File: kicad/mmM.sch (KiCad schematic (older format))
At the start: 29 parts, among them P1 AREF, P4 ICSP, P5 FTDI, SW1 Reset, SW2 INT0, SW3 INT1, U7 ATMEGA328P-AU-ND, X1 16MHz

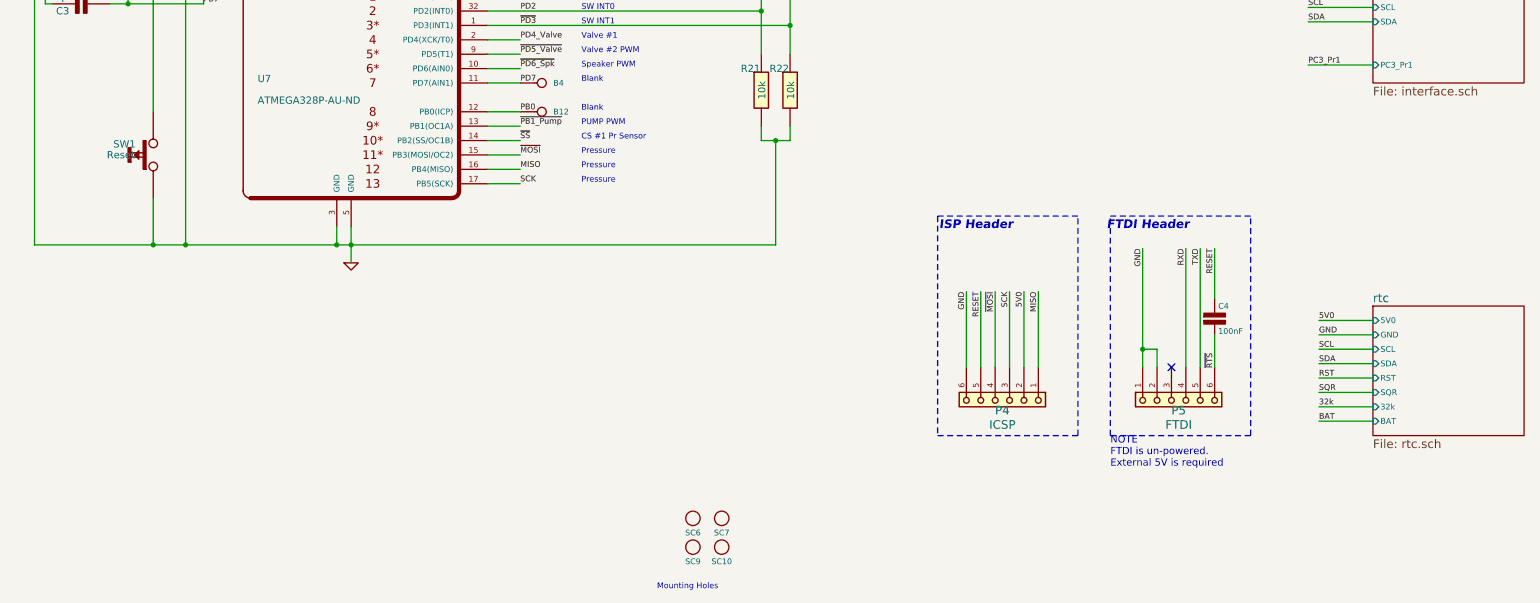
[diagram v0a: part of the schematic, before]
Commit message: added Cap across RST sw. Fresh Gerbers, PDF. Final v1 ready for prototype
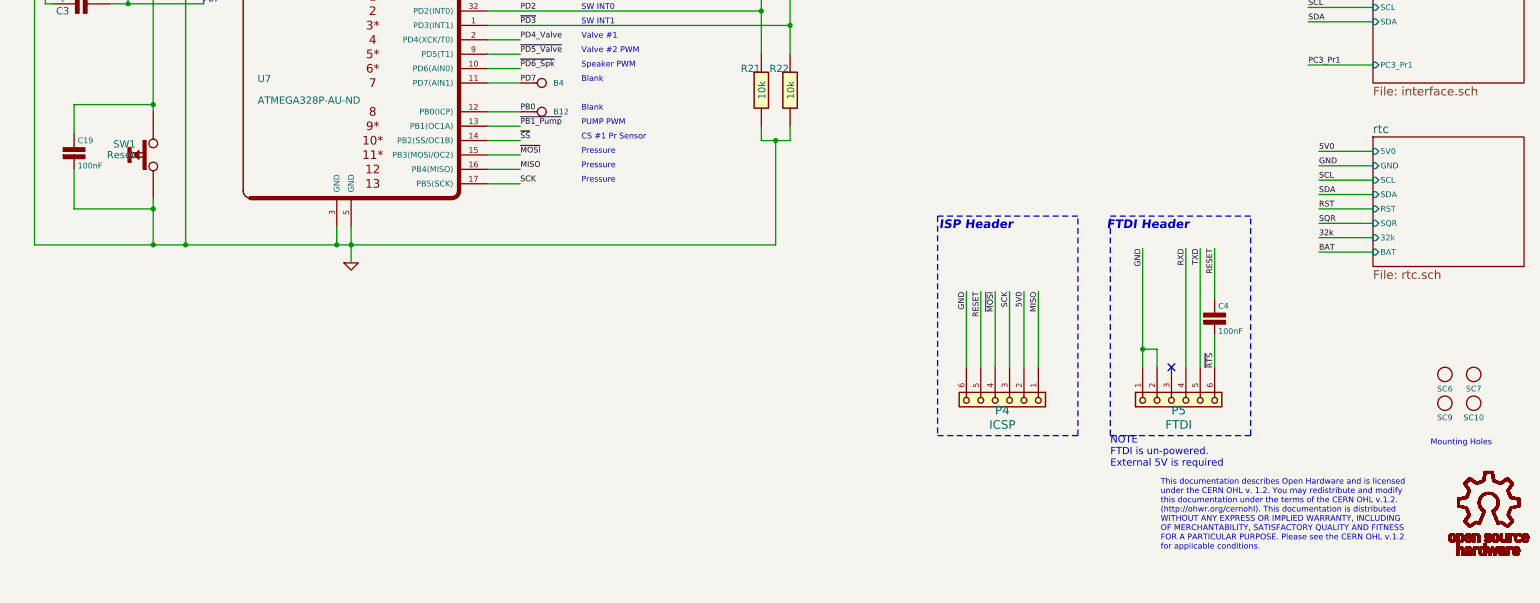
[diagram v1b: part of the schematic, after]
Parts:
- added C19: 100nF, mmM:c_0805, symbol C
- added M1: OSHW-LOGO, OSHW-LOGO, symbol OSHW-LOGO
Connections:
- net GND: now also C19.2
- net RESET: now also C19.1
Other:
- note added: "This documentation describes Open Hardware and is licensed \nunder the CERN OHL v. 1.2. You may redistribute and modify \nthis documentation under the terms of the CERN OHL v.1.2. \n(http://ohwr.org/cernohl). This documentation is distributed\nWITHOUT ANY EXPRESS OR IMPLIED WARRANTY, INCLUDING \nOF MERCHANTABILITY, SATISFACTORY QUALITY AND FITNESS\nFOR A PARTICULAR PURPOSE. Please see the CERN OH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"
- moved on the sheet: SC10, SC6, SC7, SC9
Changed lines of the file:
@@
 encoding utf-8
 Sheet 1 4
-Title "uControl_mini"
-Date "2015 July 09, Thursday"
+Title "mmMercury : Blood Pressure Measurement Platform"
+Date "2015-12-27"
 Rev "1"
 Comp "WyoLum"
@@
 Text Notes 4550 3450 0    40   ~ 0
 SW INT1
-Text Notes 5075 7375 0    40   ~ 0
+Text Notes 10450 6375 0    40   ~ 0
 Mounting Holes
 Text Label 9775 825  0    40   ~ 0
@@
 $EndSheet
 $Sheet
-S 10050 5400 1050 900
+S 10050 4225 1050 900
 U 4E1FEA4E
 F0 "rtc" 60
 F1 "rtc.sch" 60
-F2 "GND" I L 10050 5600 40
-F3 "SDA" I L 10050 5800 40
-F4 "SCL" I L 10050 5700 40
-F5 "5V0" I L 10050 5500 40
-F6 "RST" I L 10050 5900 40
-F7 "32k" I L 10050 6100 40
-F8 "BAT" I L 10050 6200 40
-F9 "SQR" I L 10050 6000 40
+F2 "GND" I L 10050 4425 40
+F3 "SDA" I L 10050 4625 40
+F4 "SCL" I L 10050 4525 40
+F5 "5V0" I L 10050 4325 40
+F6 "RST" I L 10050 4725 40
+F7 "32k" I L 10050 4925 40
+F8 "BAT" I L 10050 5025 40
+F9 "SQR" I L 10050 4825 40
 $EndSheet
 Text Label 1025 2550 0    40   ~ 0
@@
 PB6
 $Comp
-L GND #PWR01
+L GND #PWR3
 U 1 1 4F5AFC62
 P 2950 5100
-F 0 "#PWR01" H 2950 5100 30  0001 C CNN
+F 0 "#PWR3" H 2950 5100 30  0001 C CNN
 F 1 "GND" H 2950 5030 30  0001 C CNN
 F 2 "" H 2950 5100 60  0001 C CNN
@@
 	1    0    0    -1
 $EndComp
-Text Label 9675 6200 0    40   ~ 0
+Text Label 9675 5025 0    40   ~ 0
 BAT
-Text Label 9675 6100 0    40   ~ 0
+Text Label 9675 4925 0    40   ~ 0
 32k
-Text Label 9675 6000 0    40   ~ 0
+Text Label 9675 4825 0    40   ~ 0
 SQR
-Text Label 9675 5900 0    40   ~ 0
+Text Label 9675 4725 0    40   ~ 0
 RST
-Text Label 9675 5600 0    40   ~ 0
+Text Label 9675 4425 0    40   ~ 0
 GND
-Text Label 9675 5800 0    40   ~ 0
+Text Label 9675 4625 0    40   ~ 0
 SDA
-Text Label 9675 5700 0    40   ~ 0
+Text Label 9675 4525 0    40   ~ 0
 SCL
-Text Label 9675 5500 0    40   ~ 0
+Text Label 9675 4325 0    40   ~ 0
 5V0
 Text Label 1575 2250 1    40   ~ 0
@@
 Blank
 $Comp
-L PWR_FLAG #FLG02
+L PWR_FLAG #FLG1
 U 1 1 520CA632
 P 725 2475
-F 0 "#FLG02" H 725 2745 30  0001 C CNN
+F 0 "#FLG1" H 725 2745 30  0001 C CNN
 F 1 "PWR_FLAG" H 725 2705 30  0000 C CNN
 F 2 "" H 725 2475 60  0000 C CNN
@@
 	3900 2750 4800 2750
 Wire Wire Line
-	9675 6200 10050 6200
-Wire Wire Line
-	9675 6100 10050 6100
-Wire Wire Line
-	9675 5900 10050 5900
+	9675 5025 10050 5025
+Wire Wire Line
+	9675 4925 10050 4925
+Wire Wire Line
+	9675 4725 10050 4725
 Wire Wire Line
 	1400 3250 1400 3300
@@
 	2000 2250 1575 2250
 Wire Wire Line
-	9675 5800 10050 5800
-Wire Wire Line
-	9675 5500 10050 5500
+	9675 4625 10050 4625
+Wire Wire Line
+	9675 4325 10050 4325
 Wire Wire Line
 	3900 3350 5800 3350
@@
 	4800 650  4800 1200
 Wire Wire Line
-	9675 5700 10050 5700
-Wire Wire Line
-	9675 5600 10050 5600
+	9675 4525 10050 4525
+Wire Wire Line
+	9675 4425 10050 4425
 Wire Wire Line
 	1575 1700 1575 4050
@@
 	4125 2550 3900 2550
 Wire Wire Line
-	9675 6000 10050 6000
+	9675 4825 10050 4825
 Wire Wire Line
 	725  2550 2000 2550
@@
 Connection ~ 2900 1225
 $Comp
-L GND #PWR03
+L GND #PWR1
 U 1 1 520F2321
 P 3250 1725
-F 0 "#PWR03" H 3250 1725 30  0001 C CNN
+F 0 "#PWR1" H 3250 1725 30  0001 C CNN
 F 1 "GND" H 3250 1655 30  0001 C CNN
 F 2 "" H 3250 1725 60  0001 C CNN
@@
 L SCREW SC6
 U 1 1 522315DB
-P 5325 6875
-F 0 "SC6" H 5325 6775 40  0000 C CNN
-F 1 "SCREW" H 5325 6975 40  0001 C CNN
-F 2 "mmM:vite_3mm" H 5325 7075 40  0001 C CNN
-F 3 "" H 5325 6875 60  0001 C CNN
-	1    5325 6875
+P 10550 5875
+F 0 "SC6" H 10550 5775 40  0000 C CNN
+F 1 "SCREW" H 10550 5975 40  0001 C CNN
+F 2 "mmM:vite_3mm" H 10550 6075 40  0001 C CNN
+F 3 "" H 10550 5875 60  0001 C CNN
+	1    10550 5875
 	1    0    0    -1
 $EndComp
@@
 L SCREW SC9
 U 1 1 522315E1
-P 5325 7075
-F 0 "SC9" H 5325 6975 40  0000 C CNN
-F 1 "SCREW" H 5325 7175 40  0001 C CNN
-F 2 "mmM:vite_3mm" H 5325 7275 40  0001 C CNN
-F 3 "" H 5325 7075 60  0001 C CNN
-	1    5325 7075
+P 10550 6075
+F 0 "SC9" H 10550 5975 40  0000 C CNN
+F 1 "SCREW" H 10550 6175 40  0001 C CNN
+F 2 "mmM:vite_3mm" H 10550 6275 40  0001 C CNN
+F 3 "" H 10550 6075 60  0001 C CNN
+	1    10550 6075
 	1    0    0    -1
 $EndComp
@@
 L SCREW SC7
 U 1 1 522315F3
-P 5525 6875
-F 0 "SC7" H 5525 6775 40  0000 C CNN
-F 1 "SCREW" H 5525 6975 40  0001 C CNN
-F 2 "mmM:vite_3mm" H 5525 7075 40  0001 C CNN
-F 3 "" H 5525 6875 60  0001 C CNN
-	1    5525 6875
+P 10750 5875
+F 0 "SC7" H 10750 5775 40  0000 C CNN
+F 1 "SCREW" H 10750 5975 40  0001 C CNN
+F 2 "mmM:vite_3mm" H 10750 6075 40  0001 C CNN
+F 3 "" H 10750 5875 60  0001 C CNN
+	1    10750 5875
 	1    0    0    -1
 $EndComp
@@
 L SCREW SC10
 U 1 1 522315F9
-P 5525 7075
-F 0 "SC10" H 5525 6975 40  0000 C CNN
-F 1 "SCREW" H 5525 7175 40  0001 C CNN
-F 2 "mmM:vite_3mm" H 5525 7275 40  0001 C CNN
-F 3 "" H 5525 7075 60  0001 C CNN
-	1    5525 7075
+P 10750 6075
+F 0 "SC10" H 10750 5975 40  0000 C CNN
+F 1 "SCREW" H 10750 6175 40  0001 C CNN
+F 2 "mmM:vite_3mm" H 10750 6275 40  0001 C CNN
+F 3 "" H 10750 6075 60  0001 C CNN
+	1    10750 6075
 	1    0    0    -1
 $EndComp
@@
 SCL
 $Comp
-L GND #PWR04
+L GND #PWR2
 U 1 1 55E8B5A9
 P 1200 2250
-F 0 "#PWR04" H 1200 2250 30  0001 C CNN
+F 0 "#PWR2" H 1200 2250 30  0001 C CNN
 F 1 "GND" H 1200 2180 30  0001 C CNN
 F 2 "" H 1200 2250 60  0001 C CNN
@@
 	1    0    0    -1
 $EndComp
+$Comp
+L C C19
+U 1 1 567FE54D
+P 1025 4325
+F 0 "C19" H 1050 4400 40  0000 L CNN
+F 1 "100nF" H 1050 4225 40  0000 L CNN
+F 2 "mmM:c_0805" H 1025 4325 60  0001 C CNN
+F 3 "" H 1025 4325 60  0000 C CNN
+F 4 "CL21B104KCC5PNC" H 1025 4325 60  0001 C CNN "manf#"
+	1    1025 4325
+	1    0    0    -1
+$EndComp
+Wire Wire Line
+	1025 4000 1025 4200
+Wire Wire Line
+	1025 4000 1575 4000
+Connection ~ 1575 4000
+Wire Wire Line
+	1025 4450 1025 4725
+Wire Wire Line
+	1025 4725 1575 4725
+Connection ~ 1575 4725
+$Comp
+L OSHW-LOGO M1
+U 1 1 5680B029
+P 10850 6825
+F 0 "M1" H 10850 6825 50  0001 C CNN
+F 1 "OSHW-LOGO" H 10850 6825 50  0001 C CNN
+F 2 "OSHW-LOGO" H 10880 6975 20  0001 C CNN
+F 3 "" H 10850 6825 60  0000 C CNN
+	1    10850 6825
+	1    0    0    -1
+$EndComp
+Text Notes 8575 7100 0    40   ~ 0
+This documentation describes Open Hardware and is licensed \nunder the CERN OHL v. 1.2. You may redistribute and modify \nthis documentation under the terms of the CERN OHL v.1.2. \n(http://ohwr.org/cernohl). This documentation is distributed\nWITHOUT ANY EXPRESS OR IMPLIED WARRANTY, INCLUDING \nOF MERCHANTABILITY, SATISFACTORY QUALITY AND FITNESS\nFOR A PARTICULAR PURPOSE. Please see the CERN OHL v.1.2\nfor applicable conditions.
 $EndSCHEMATC

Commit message: made a pretty schematic, fresh symbols
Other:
- moved on the sheet: R22, SW3

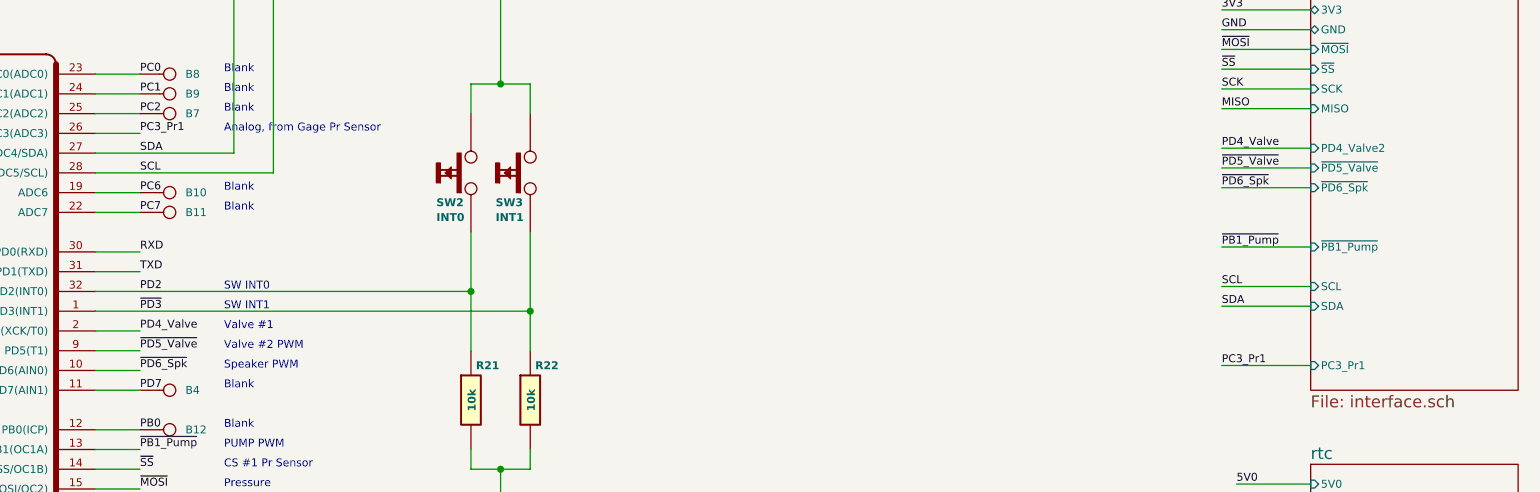
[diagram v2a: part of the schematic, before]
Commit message: schematic label errors corrected, Git issue #2
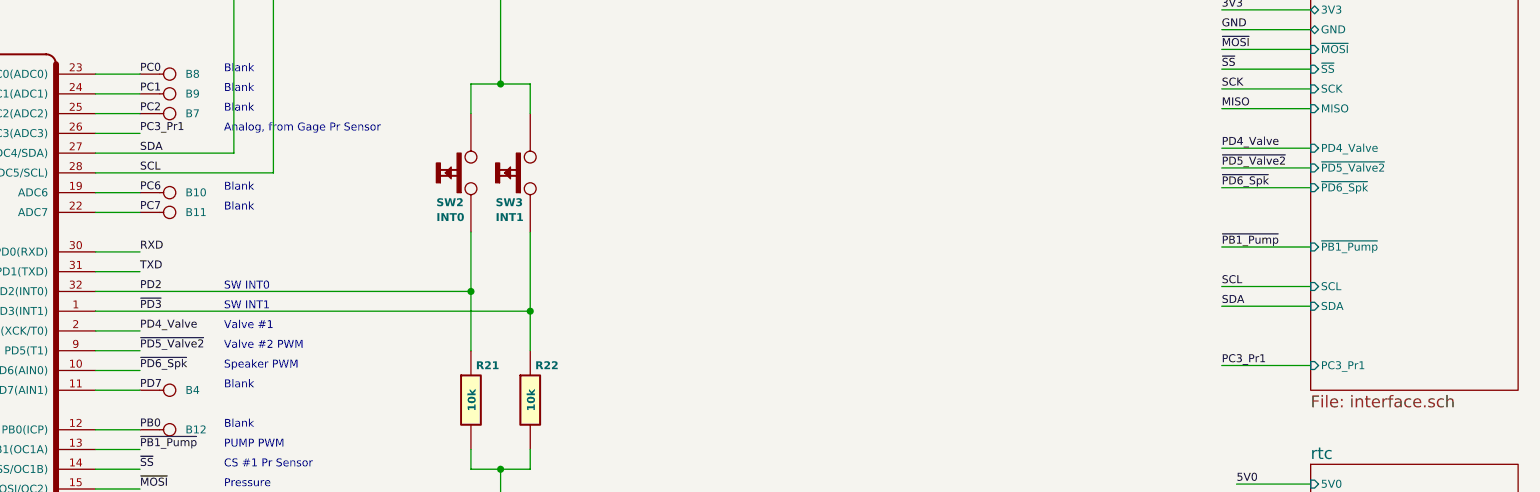
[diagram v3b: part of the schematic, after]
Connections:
- net ~PD5_Valve renamed ~PD5_Valve2
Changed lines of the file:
@@
 F5 "GND" B L 10050 2025 40
 F6 "5V0" B L 10050 1825 40
-F7 "~PD5_Valve" I L 10050 2725 40
+F7 "~PD5_Valve2" I L 10050 2725 40
 F8 "~MOSI" I L 10050 2125 40
 F9 "~SS" I L 10050 2225 40
@@
 F11 "3V3" B L 10050 1925 40
 F12 "~PB1_Pump" I L 10050 3125 40
-F13 "PD4_Valve2" I L 10050 2625 40
+F13 "PD4_Valve" I L 10050 2625 40
 F14 "~PD6_Spk" I L 10050 2825 40
 F15 "SCL" I L 10050 3325 40
@@
 PC3_Pr1
 Text Label 9600 2725 0    40   ~ 0
-~PD5_Valve
+~PD5_Valve2
 Text Label 9600 2025 0    40   ~ 0
 GND
@@
 RESET
 Text Label 4125 3650 0    40   ~ 0
-~PD5_Valve
+~PD5_Valve2
 Text Label 4125 3750 0    40   ~ 0
 ~PD6_Spk
